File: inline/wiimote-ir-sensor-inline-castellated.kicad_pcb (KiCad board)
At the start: 2 copper layers, 13 x 16 mm, 10 parts, among them J1 Conn_01x04_Pin, U2 AP2112-3.3V, X1 SG3225CAN 24.0000M-TJGA3

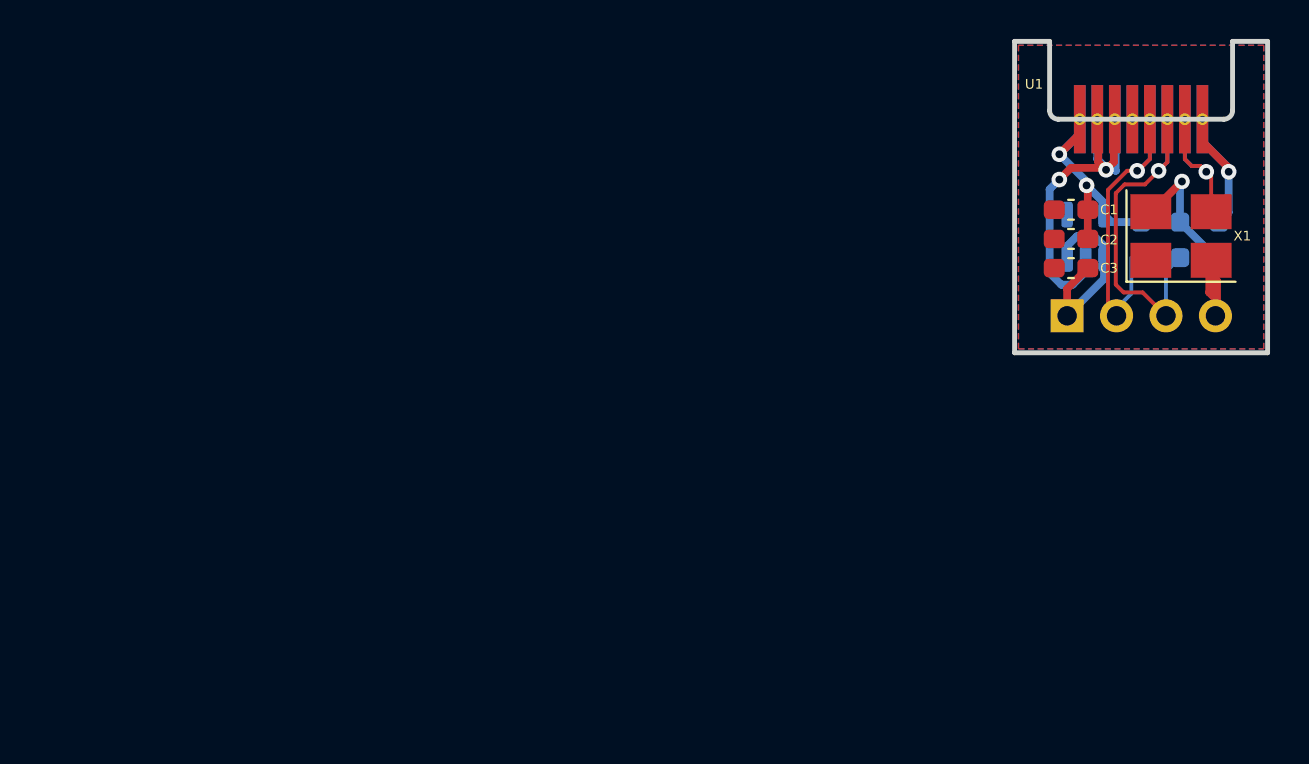
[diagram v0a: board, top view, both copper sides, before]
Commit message: Update castellated board with proper SDA/SCL labels
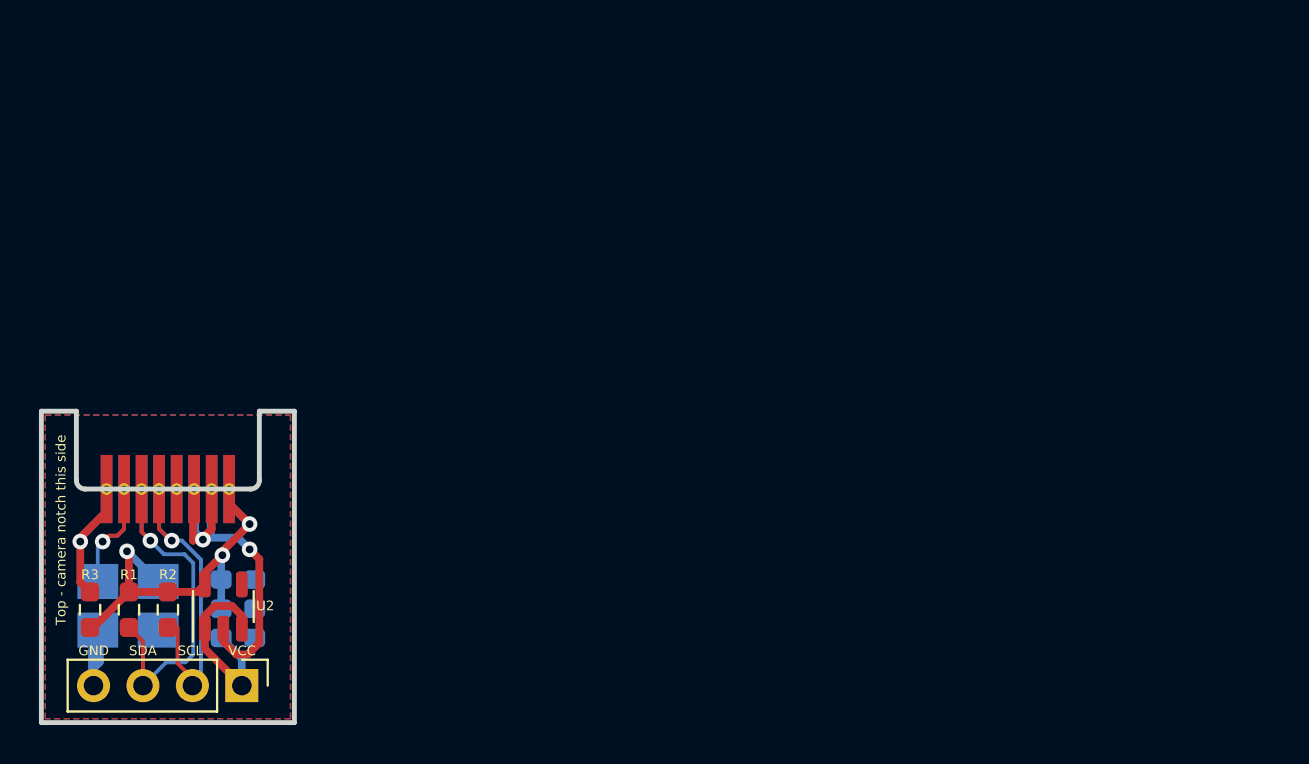
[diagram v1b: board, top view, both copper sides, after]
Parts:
- C1, C2, C3, U1, X1: moved to B.Cu
- J1, R1, R2, R3, U2: moved to F.Cu
- moved R3 61.0 mm to (102.5, 110.2)
- moved X1 57.3 mm to (104.5, 110.0), turned to 180 degrees
- moved R1 57.2 mm to (104.5, 110.2)
- moved R2 53.5 mm to (106.5, 110.2)
- moved U1 53.5 mm to (106.5, 101.5), turned to 180 degrees
- moved U2 48.2 mm to (109.3, 110.0)
- moved C1 46.8 mm to (110.1, 108.7), turned to 0 degrees
- moved C2 46.8 mm to (110.1, 110.2), turned to 0 degrees
- moved C3 46.8 mm to (110.1, 111.7), turned to 0 degrees
- moved J1 46.5 mm to (110.3, 114.1)
